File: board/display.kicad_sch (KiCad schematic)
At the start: 1 part, among them U1 Waveshare_LCD_Module_2.4in

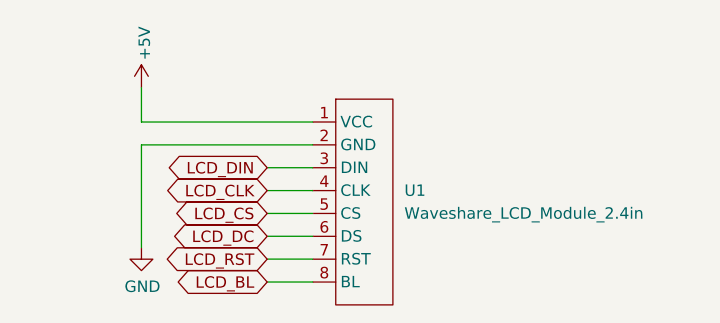
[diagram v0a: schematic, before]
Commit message: updated to Crane V2 Rev A
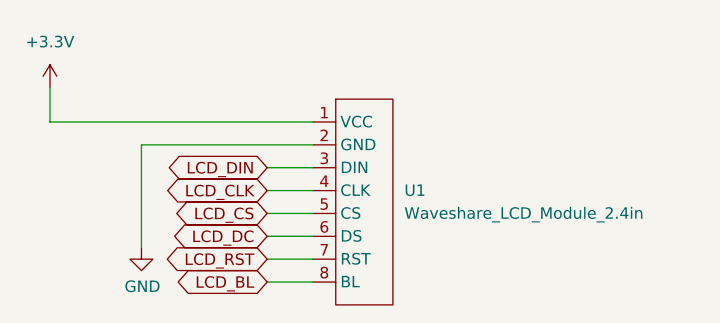
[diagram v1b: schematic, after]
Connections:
- net +5V renamed +3V3
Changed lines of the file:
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@@
-(kicad_sch (version 20211123) (generator eeschema)
+(kicad_sch (version 20230121) (generator eeschema)
   (paper "A4")
   (wire (pts (xy 148.59 93.98) (xy 153.67 93.98))
-    (stroke (width 0) (type default) (color 0 0 0 0))
+    (stroke (width 0) (type default))
+  )
+  (wire (pts (xy 124.46 72.39) (xy 124.46 76.2))
+    (stroke (width 0) (type default))
   )
   (wire (pts (xy 148.59 91.44) (xy 153.67 91.44))
-    (stroke (width 0) (type default) (color 0 0 0 0))
-  )
-  (wire (pts (xy 134.62 76.2) (xy 134.62 72.39))
-    (stroke (width 0) (type default) (color 0 0 0 0))
+    (stroke (width 0) (type default))
   )
   (wire (pts (xy 148.59 88.9) (xy 153.67 88.9))
-    (stroke (width 0) (type default) (color 0 0 0 0))
+    (stroke (width 0) (type default))
   )
-  (wire (pts (xy 153.67 76.2) (xy 134.62 76.2))
-    (stroke (width 0) (type default) (color 0 0 0 0))
+  (wire (pts (xy 124.46 76.2) (xy 153.67 76.2))
+    (stroke (width 0) (type default))
   )
   (wire (pts (xy 148.59 86.36) (xy 153.67 86.36))
-    (stroke (width 0) (type default) (color 0 0 0 0))
+    (stroke (width 0) (type default))
   )
   (wire (pts (xy 153.67 78.74) (xy 134.62 78.74))
-    (stroke (width 0) (type default) (color 0 0 0 0))
+    (stroke (width 0) (type default))
   )
   (wire (pts (xy 148.59 83.82) (xy 153.67 83.82))
-    (stroke (width 0) (type default) (color 0 0 0 0))
+    (stroke (width 0) (type default))
   )
   (wire (pts (xy 148.59 81.28) (xy 153.67 81.28))
-    (stroke (width 0) (type default) (color 0 0 0 0))
+    (stroke (width 0) (type default))
   )
   (wire (pts (xy 134.62 78.74) (xy 134.62 90.17))
-    (stroke (width 0) (type solid) (color 0 0 0 0))
+    (stroke (width 0) (type solid))
   )
   (global_label "LCD_DIN" (shape bidirectional) (at 148.59 81.28 180) (fields_autoplaced)
     (effects (font (size 1.27 1.27)) (justify right))
-    (property "Intersheet References" "${INTERSHEET_REFS}" (id 0) (at 138.2454 81.2006 0)
+    (property "Intersheetrefs" "${INTERSHEET_REFS}" (at 138.2454 81.2006 0)
       (effects (font (size 1.27 1.27)) (justify right) hide)
     )
@@
   (global_label "LCD_BL" (shape bidirectional) (at 148.59 93.98 180) (fields_autoplaced)
     (effects (font (size 1.27 1.27)) (justify right))
-    (property "Intersheet References" "${INTERSHEET_REFS}" (id 0) (at 139.1526 93.9006 0)
+    (property "Intersheetrefs" "${INTERSHEET_REFS}" (at 139.1526 93.9006 0)
       (effects (font (size 1.27 1.27)) (justify right) hide)
     )
@@
   (global_label "LCD_RST" (shape bidirectional) (at 148.59 91.44 180) (fields_autoplaced)
     (effects (font (size 1.27 1.27)) (justify right))
-    (property "Intersheet References" "${INTERSHEET_REFS}" (id 0) (at 138.0035 91.3606 0)
+    (property "Intersheetrefs" "${INTERSHEET_REFS}" (at 138.0035 91.3606 0)
       (effects (font (size 1.27 1.27)) (justify right) hide)
     )
@@
   (global_label "LCD_DC" (shape bidirectional) (at 148.59 88.9 180) (fields_autoplaced)
     (effects (font (size 1.27 1.27)) (justify right))
-    (property "Intersheet References" "${INTERSHEET_REFS}" (id 0) (at 138.9107 88.8206 0)
+    (property "Intersheetrefs" "${INTERSHEET_REFS}" (at 138.9107 88.8206 0)
       (effects (font (size 1.27 1.27)) (justify right) hide)
     )
@@
   (global_label "LCD_CLK" (shape bidirectional) (at 148.59 83.82 180) (fields_autoplaced)
     (effects (font (size 1.27 1.27)) (justify right))
-    (property "Intersheet References" "${INTERSHEET_REFS}" (id 0) (at 137.8826 83.7406 0)
+    (property "Intersheetrefs" "${INTERSHEET_REFS}" (at 137.8826 83.7406 0)
       (effects (font (size 1.27 1.27)) (justify right) hide)
     )
@@
   (global_label "LCD_CS" (shape bidirectional) (at 148.59 86.36 180) (fields_autoplaced)
     (effects (font (size 1.27 1.27)) (justify right))
-    (property "Intersheet References" "${INTERSHEET_REFS}" (id 0) (at 138.9712 86.2806 0)
+    (property "Intersheetrefs" "${INTERSHEET_REFS}" (at 138.9712 86.2806 0)
       (effects (font (size 1.27 1.27)) (justify right) hide)
     )
   )
-  (symbol (lib_id "power:GND") (at 134.62 90.17 0) (unit 1)
-    (in_bom yes) (on_board yes)
-    (property "Reference" "#PWR011" (id 0) (at 134.62 96.52 0)
+  (symbol (lib_id "power:+3.3V") (at 124.46 72.39 0) (unit 1)
+    (in_bom yes) (on_board yes) (dnp no) (fields_autoplaced)
+    (property "Reference" "#PWR011" (at 124.46 76.2 0)
       (effects (font (size 1.27 1.27)) hide)
     )
-    (property "Value" "GND" (id 1) (at 134.7343 94.4944 0))
-    (property "Footprint" "" (id 2) (at 134.62 90.17 0))
-    (property "Datasheet" "" (id 3) (at 134.62 90.17 0))
-    (pin "1")
-  )
-  (symbol (lib_id "power:+5V") (at 134.62 72.39 0) (unit 1)
-    (in_bom yes) (on_board yes)
-    (property "Reference" "#PWR010" (id 0) (at 134.62 76.2 0)
+    (property "Value" "+3.3V" (at 124.46 67.31 0)
+      (effects (font (size 1.27 1.27)))
+    )
+    (property "Footprint" "" (at 124.46 72.39 0)
       (effects (font (size 1.27 1.27)) hide)
     )
-    (property "Value" "+5V" (id 1) (at 134.9756 69.342 90)
+    (property "Datasheet" "" (at 124.46 72.39 0)
+      (effects (font (size 1.27 1.27)) hide)
+    )
+    (pin "1")
+    (instances
+      (project "hoatzin"
+        (path "/7df740c4-7396-4973-b091-33b55deb1d43/afbb6b34-d17e-4b2d-85e1-26d09171c0ec"
+          (reference "#PWR011") (unit 1)
+        )
+      )
+      (project "crane"
+        (path "/e63e39d7-6ac0-4ffd-8aa3-1841a4541b55/f6045514-38c2-44cb-acca-4b3bf6c6991a"
+          (reference "#PWR016") (unit 1)
+        )
+        (path "/e63e39d7-6ac0-4ffd-8aa3-1841a4541b55/83ccfa5a-5eee-4699-b79a-ea5dab229415"
+          (reference "#PWR032") (unit 1)
+        )
+      )
+    )
+  )
+  (symbol (lib_id "power:GND") (at 134.62 90.17 0) (unit 1)
+    (in_bom yes) (on_board yes) (dnp no)
+    (property "Reference" "#PWR011" (at 134.62 96.52 0)
+      (effects (font (size 1.27 1.27)) hide)
+    )
+    (property "Value" "GND" (at 134.7343 94.4944 0)
+      (effects (font (size 1.27 1.27)))
+    )
+    (property "Footprint" "" (at 134.62 90.17 0)
+      (effects (font (size 1.27 1.27)))
+    )
+    (property "Datasheet" "" (at 134.62 90.17 0)
+      (effects (font (size 1.27 1.27)))
+    )
+    (pin "1")
+    (instances
+      (project "crane"
+        (path "/e63e39d7-6ac0-4ffd-8aa3-1841a4541b55/83ccfa5a-5eee-4699-b79a-ea5dab229415"
+          (reference "#PWR011") (unit 1)
+        )
+      )
+    )
+  )
+  (symbol (lib_id "Waveshare_LCD_Module:Waveshare_LCD_Module_2.4in") (at 156.21 72.39 0) (unit 1)
+    (in_bom yes) (on_board yes) (dnp no) (fields_autoplaced)
+    (property "Reference" "U1" (at 163.83 83.8199 0)
       (effects (font (size 1.27 1.27)) (justify left))
     )
-    (property "Footprint" "" (id 2) (at 134.62 72.39 0))
-    (property "Datasheet" "" (id 3) (at 134.62 72.39 0))
-    (pin "1")
-  )
-  (symbol (lib_id "Waveshare_LCD_Module:Waveshare_LCD_Module_2.4in") (at 156.21 72.39 0) (unit 1)
-    (in_bom yes) (on_board yes) (fields_autoplaced)
-    (property "Reference" "U1" (id 0) (at 163.83 83.8199 0)
+    (property "Value" "Waveshare_LCD_Module_2.4in" (at 163.83 86.3599 0)
       (effects (font (size 1.27 1.27)) (justify left))
     )
-    (property "Value" "Waveshare_LCD_Module_2.4in" (id 1) (at 163.83 86.3599 0)
-      (effects (font (size 1.27 1.27)) (justify left))
-    )
-    (property "Footprint" "Waveshare_LCD_Module:Waveshare_LCD_Module_2_4in" (id 2) (at 156.21 72.39 0)
+    (property "Footprint" "Waveshare_LCD_Module:Waveshare_LCD_Module_2_4in" (at 156.21 72.39 0)
       (effects (font (size 1.27 1.27)) hide)
     )
-    (property "Datasheet" "" (id 3) (at 156.21 72.39 0)
+    (property "Datasheet" "" (at 156.21 72.39 0)
       (effects (font (size 1.27 1.27)) hide)
     )
@@
     (pin "7")
     (pin "8")
+    (instances
+      (project "crane"
+        (path "/e63e39d7-6ac0-4ffd-8aa3-1841a4541b55/83ccfa5a-5eee-4699-b79a-ea5dab229415"
+          (reference "U1") (unit 1)
+        )
+      )
+    )
   )
 )

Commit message: removed software folder
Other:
- title: (none) -> Crane V2.0 Rev A
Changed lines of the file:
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@@
 (kicad_sch (version 20230121) (generator eeschema)
   (paper "A4")
+  (title_block
+    (title "Crane V2.0 Rev A")
+  )
   (wire (pts (xy 148.59 93.98) (xy 153.67 93.98))
     (stroke (width 0) (type default))
